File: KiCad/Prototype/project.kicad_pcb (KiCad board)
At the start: 2 copper layers, 166 x 70 mm, 74 parts, among them J1 Barrel_Jack, J10 POT 2, J11 POT 3, J12 POT 4, J13 POT 5, J14 PRESSURE, J15 MIDI IN, J16 MIDI OUT, J17 POT 6, J18 POT 7, J19 POT 8, J2 USB_B, J20 TTL MIDI, J3 ICSP, J4 BANK 0..7, J5 BANK 8..15, J6 EXPRESSION, J7 SUSTAIN, J8 PD6/ADC9/SPEAKER, J9 POT 1, Q1 PMV48XP,215, SW1 RESET, U1 74LS75, U10 HCPL-0600, U2 LMV358, U3 AMS1117-5.0, U4 ATMEGA32U4-AU, U5 74HC138, U6 74HC138, U7 74HC238, U8 74HC238, U9 74HC04, Y1 16 Mhz

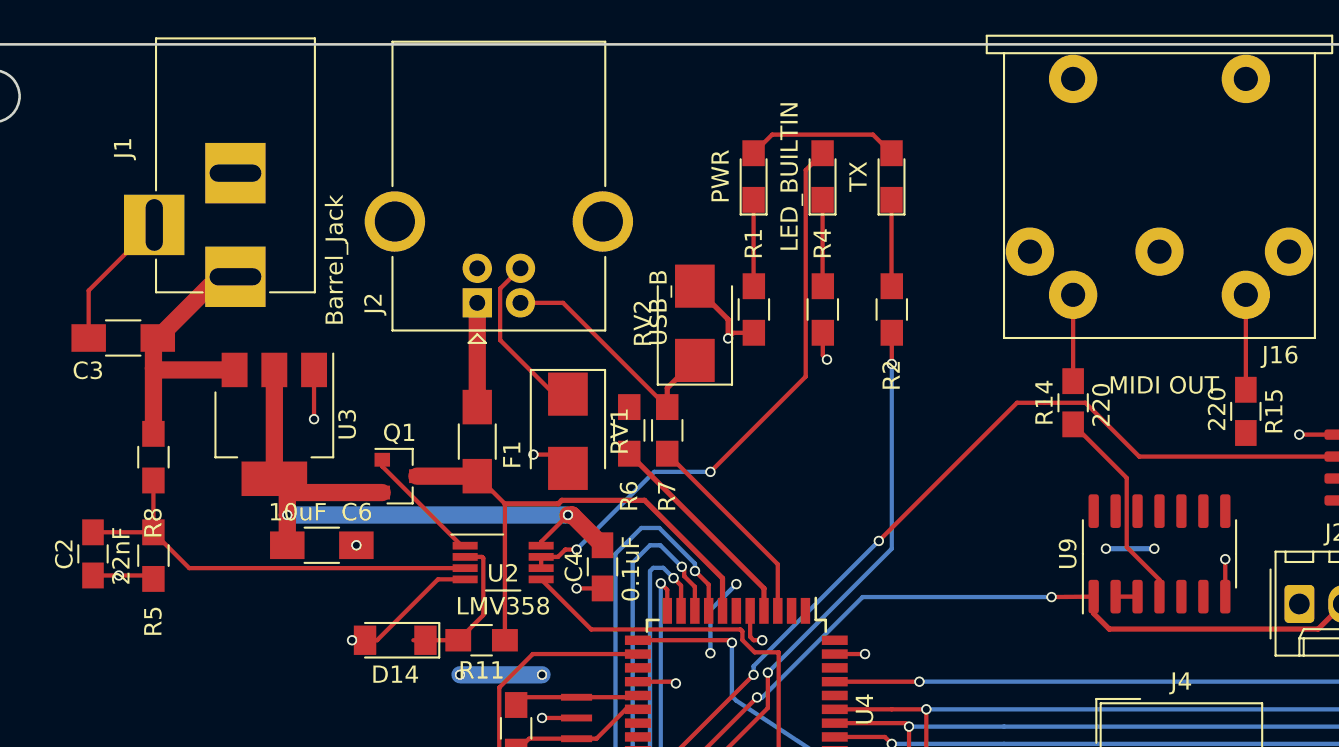
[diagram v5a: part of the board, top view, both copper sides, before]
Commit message: missing connection. silkscreen adjustments.
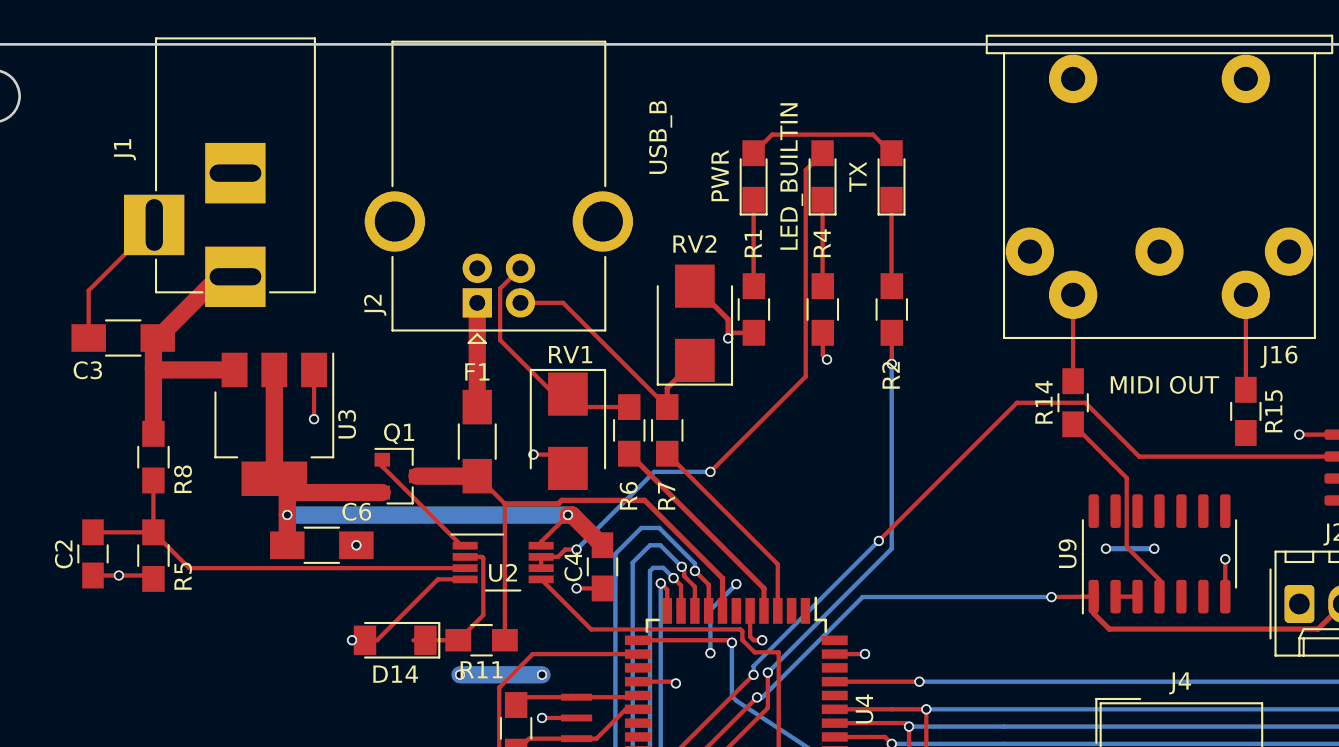
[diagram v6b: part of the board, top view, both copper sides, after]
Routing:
- net Net-(J2-Pad3): track 10.2 -> 14.1 mm

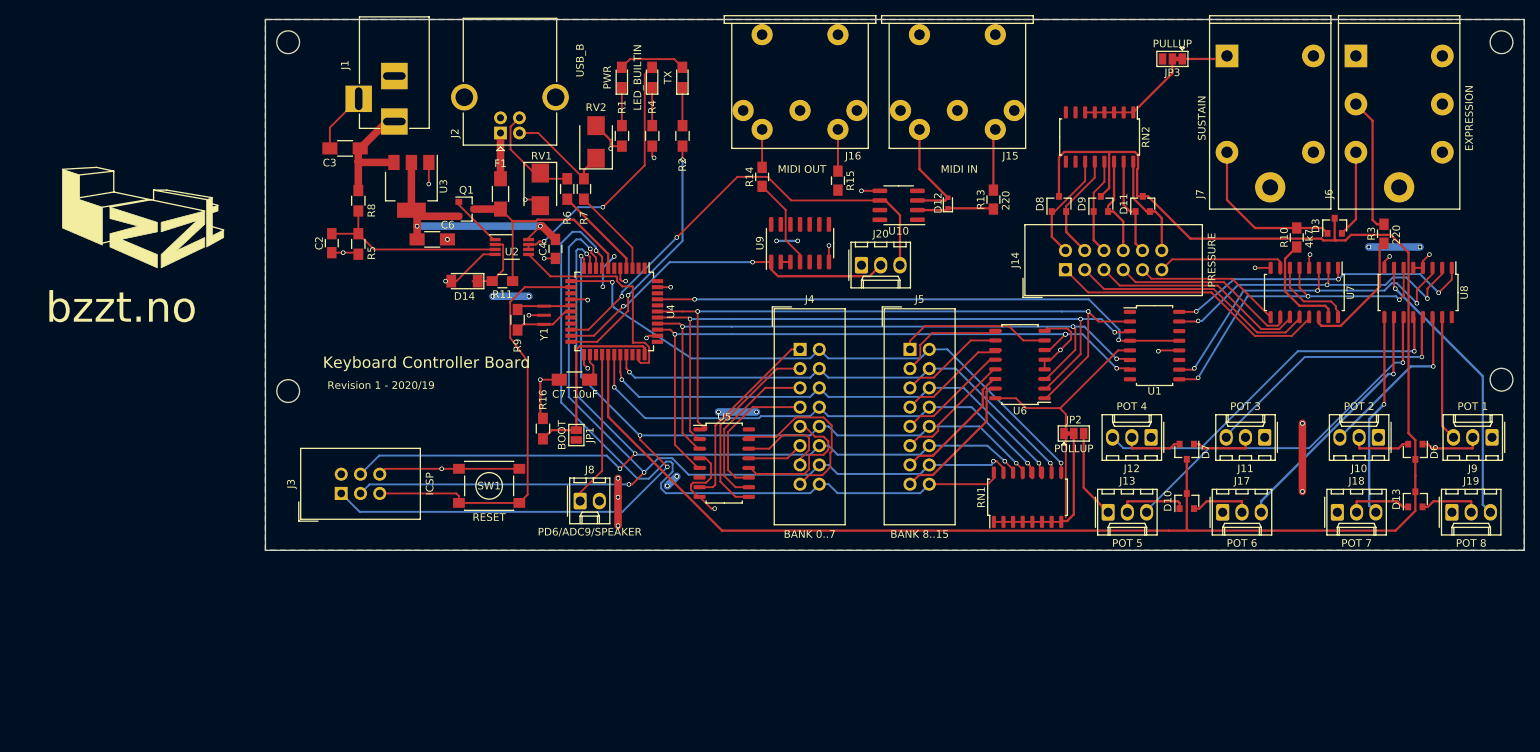
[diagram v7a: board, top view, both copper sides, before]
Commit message: Silkscreen Logo added
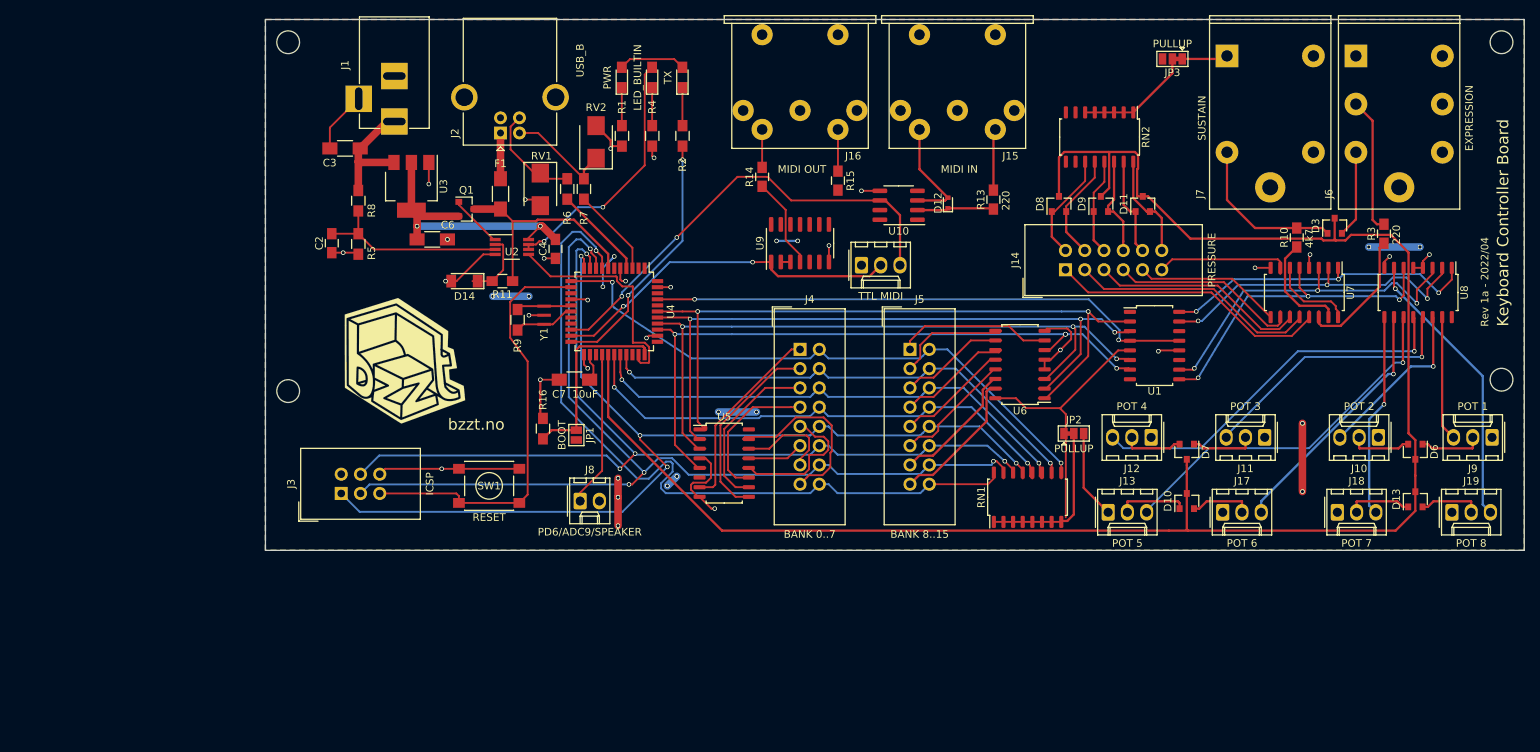
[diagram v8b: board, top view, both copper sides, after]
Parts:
- added G***: LOGO, footprints:bzzt-logo, F.Cu at (62.4, 85.0)
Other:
- board text added: "Rev 1a - 2022/04"
- board text removed: "Revision 1 - 2020/19"
